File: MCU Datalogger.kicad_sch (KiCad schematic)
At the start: 25 parts, among them U1 24LC1025, U2 DS1337S+, U3 24LC1025, U4 ATMEGA328P-AU, Y1 32.768 KHz, Y2 16MHz

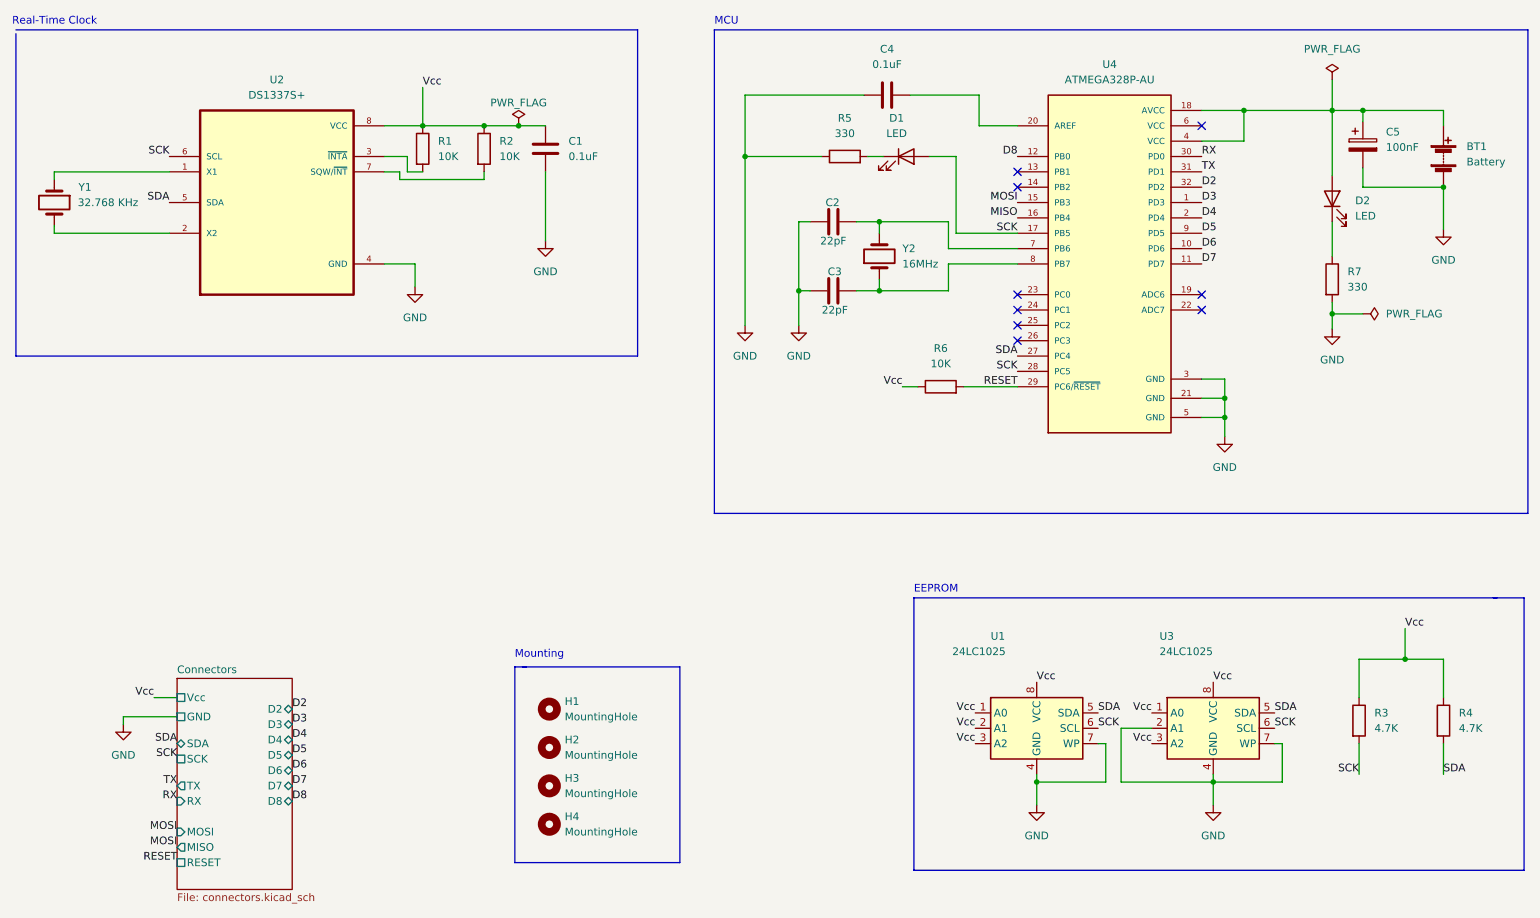
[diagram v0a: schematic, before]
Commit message: Fix schematic defect. SCK changed to SCL
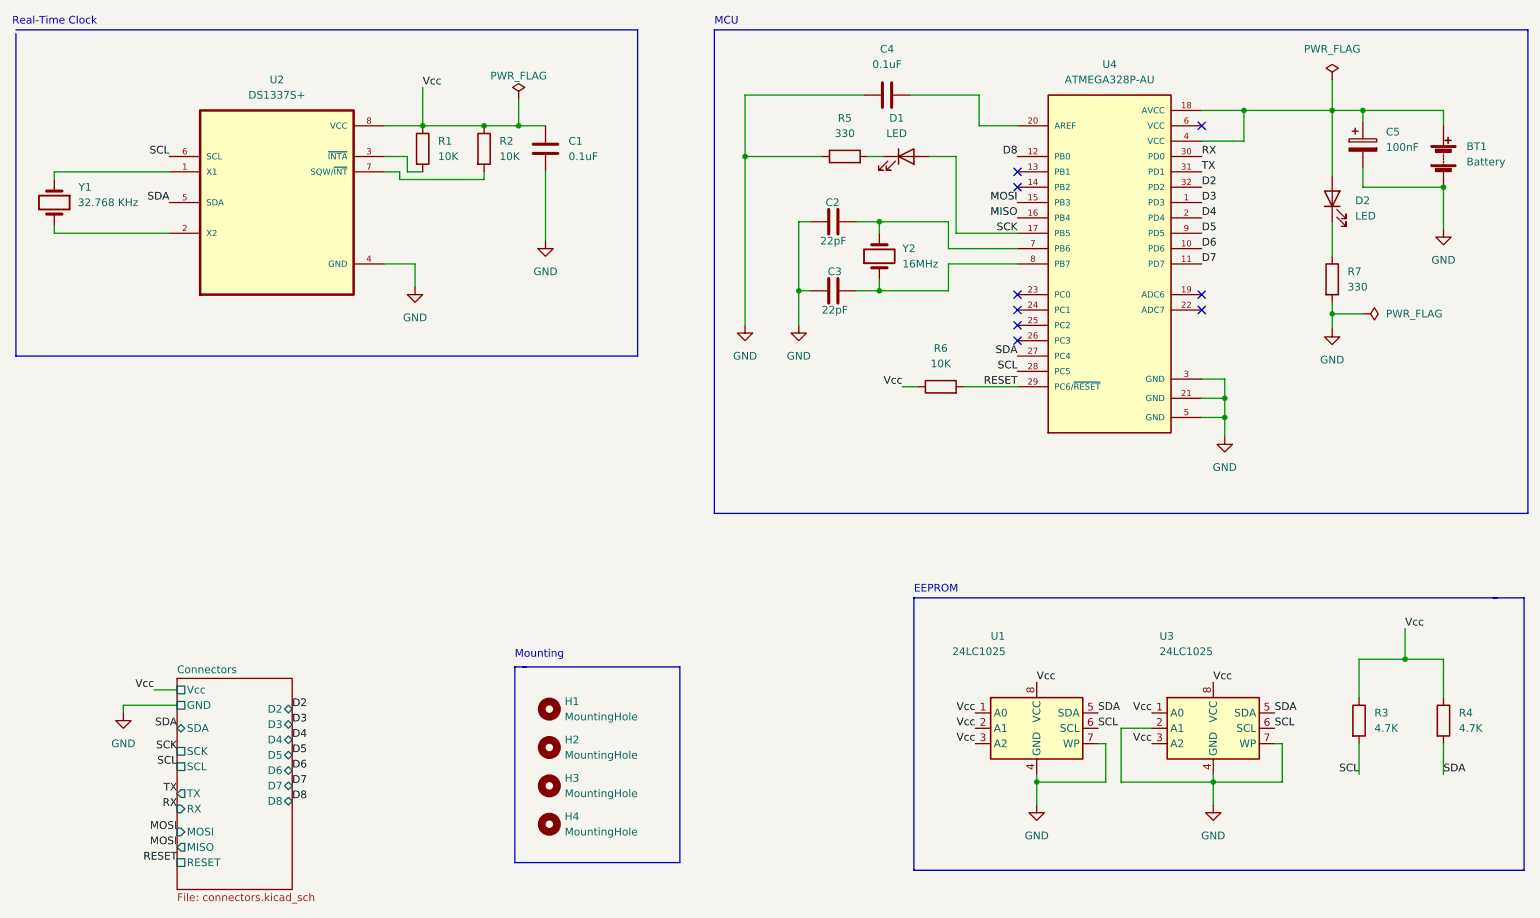
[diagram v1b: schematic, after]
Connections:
- net SCK: no longer R3.2, U1.6 (SCL), U2.6 (SCL), U3.6 (SCL), U4.28 (PC5)
- new net SCL: R3.2, U1.6 (SCL), U2.6 (SCL), U3.6 (SCL), U4.28 (PC5)
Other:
- sheet Connectors ports: added SCL; removed none
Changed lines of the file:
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@@
+    (stroke (width 0) (type default) (color 0 0 0 0))
+  )
+  (wire (pts (xy 107.315 34.29) (xy 107.315 38.735))
     (stroke (width 0) (type default) (color 0 0 0 0))
   )
@@
     (stroke (width 0) (type default) (color 0 0 0 0))
   )
+  (wire (pts (xy 41.91 135.89) (xy 41.91 134.62))
+    (stroke (width 0) (type default) (color 0 0 0 0))
+  )
   (wire (pts (xy 220.345 41.275) (xy 227.33 41.275))
     (stroke (width 0) (type default) (color 0 0 0 0))
@@
     (stroke (width 0) (type default) (color 0 0 0 0))
   )
-  (wire (pts (xy 50.8 136.525) (xy 41.91 136.525))
-    (stroke (width 0) (type default) (color 0 0 0 0))
-  )
   (wire (pts (xy 260.35 36.195) (xy 260.35 38.735))
     (stroke (width 0) (type default) (color 0 0 0 0))
@@
     (stroke (width 0) (type default) (color 0 0 0 0))
   )
+  (wire (pts (xy 41.91 134.62) (xy 50.8 134.62))
+    (stroke (width 0) (type default) (color 0 0 0 0))
+  )
   (wire (pts (xy 88.9 43.815) (xy 88.9 46.355))
     (stroke (width 0) (type default) (color 0 0 0 0))
@@
     (stroke (width 0) (type default) (color 0 0 0 0))
   )
-  (wire (pts (xy 41.91 136.525) (xy 41.91 137.795))
-    (stroke (width 0) (type default) (color 0 0 0 0))
-  )
   (polyline (pts (xy 133.985 128.27) (xy 133.985 160.655))
     (stroke (width 0) (type default) (color 0 0 0 0))
@@
     (stroke (width 0) (type default) (color 0 0 0 0))
   )
-  (wire (pts (xy 46.99 133.35) (xy 50.8 133.35))
+  (wire (pts (xy 46.99 132.08) (xy 50.8 132.08))
     (stroke (width 0) (type default) (color 0 0 0 0))
   )
@@
     (effects (font (size 1.27 1.27)) (justify left bottom))
   )
-  (label "SCK" (at 246.38 146.05 180)
-    (effects (font (size 1.27 1.27)) (justify right bottom))
-  )
   (label "TX" (at 220.345 46.355 0)
     (effects (font (size 1.27 1.27)) (justify left bottom))
@@
     (effects (font (size 1.27 1.27)) (justify right bottom))
   )
-  (label "SCK" (at 189.865 79.375 180)
+  (label "SCL" (at 189.865 79.375 180)
     (effects (font (size 1.27 1.27)) (justify right bottom))
   )
@@
     (effects (font (size 1.27 1.27)) (justify right bottom))
   )
-  (label "TX" (at 50.8 147.955 180)
+  (label "TX" (at 50.8 149.225 180)
     (effects (font (size 1.27 1.27)) (justify right bottom))
   )
@@
     (effects (font (size 1.27 1.27)) (justify left bottom))
   )
-  (label "SDA" (at 50.8 140.97 180)
+  (label "SDA" (at 50.8 138.43 180)
     (effects (font (size 1.27 1.27)) (justify right bottom))
   )
@@
     (effects (font (size 1.27 1.27)) (justify left bottom))
   )
+  (label "SCL" (at 232.41 138.43 0)
+    (effects (font (size 1.27 1.27)) (justify left bottom))
+  )
   (label "RESET" (at 189.865 81.915 180)
     (effects (font (size 1.27 1.27)) (justify right bottom))
@@
     (effects (font (size 1.27 1.27)) (justify left bottom))
   )
+  (label "SCL" (at 203.2 138.43 0)
+    (effects (font (size 1.27 1.27)) (justify left bottom))
+  )
   (label "MOSI" (at 189.865 51.435 180)
     (effects (font (size 1.27 1.27)) (justify right bottom))
@@
     (effects (font (size 1.27 1.27)) (justify right bottom))
   )
-  (label "SCK" (at 203.2 138.43 0)
-    (effects (font (size 1.27 1.27)) (justify left bottom))
-  )
   (label "SDA" (at 203.2 135.89 0)
     (effects (font (size 1.27 1.27)) (justify left bottom))
@@
     (effects (font (size 1.27 1.27)) (justify left bottom))
   )
-  (label "SCK" (at 49.53 43.815 180)
-    (effects (font (size 1.27 1.27)) (justify right bottom))
-  )
   (label "D3" (at 220.345 51.435 0)
     (effects (font (size 1.27 1.27)) (justify left bottom))
@@
     (effects (font (size 1.27 1.27)) (justify left bottom))
   )
+  (label "SCL" (at 246.38 146.05 180)
+    (effects (font (size 1.27 1.27)) (justify right bottom))
+  )
+  (label "SCL" (at 50.8 144.78 180)
+    (effects (font (size 1.27 1.27)) (justify right bottom))
+  )
+  (label "SCL" (at 49.53 43.815 180)
+    (effects (font (size 1.27 1.27)) (justify right bottom))
+  )
   (label "SCK" (at 189.865 56.515 180)
     (effects (font (size 1.27 1.27)) (justify right bottom))
@@
     (effects (font (size 1.27 1.27)) (justify left bottom))
   )
-  (label "Vcc" (at 46.99 133.35 180)
+  (label "Vcc" (at 46.99 132.08 180)
     (effects (font (size 1.27 1.27)) (justify right bottom))
   )
@@
     (effects (font (size 1.27 1.27)) (justify left bottom))
   )
-  (label "SCK" (at 50.8 143.51 180)
-    (effects (font (size 1.27 1.27)) (justify right bottom))
-  )
-  (label "RX" (at 50.8 150.495 180)
+  (label "RX" (at 50.8 151.765 180)
     (effects (font (size 1.27 1.27)) (justify right bottom))
   )
@@
     (effects (font (size 1.27 1.27)) (justify right bottom))
   )
-  (label "SCK" (at 232.41 138.43 0)
-    (effects (font (size 1.27 1.27)) (justify left bottom))
-  )
   (label "D7" (at 69.85 147.955 0)
     (effects (font (size 1.27 1.27)) (justify left bottom))
@@
     (effects (font (size 1.27 1.27)) (justify left bottom))
   )
+  (label "SCK" (at 50.8 142.24 180)
+    (effects (font (size 1.27 1.27)) (justify right bottom))
+  )
   (label "SDA" (at 260.35 146.05 0)
     (effects (font (size 1.27 1.27)) (justify left bottom))
@@
     (effects (font (size 1.27 1.27)) (justify left bottom))
   )
-  (symbol (lib_id "power:GND") (at 41.91 137.795 0) (unit 1)
-    (in_bom yes) (on_board yes) (fields_autoplaced)
-    (property "Reference" "#PWR0102" (id 0) (at 41.91 144.145 0)
-      (effects (font (size 1.27 1.27)) hide)
-    )
-    (property "Value" "GND" (id 1) (at 41.91 142.875 0))
-    (property "Footprint" "" (id 2) (at 41.91 137.795 0)
-      (effects (font (size 1.27 1.27)) hide)
-    )
-    (property "Datasheet" "" (id 3) (at 41.91 137.795 0)
+  (symbol (lib_id "power:GND") (at 41.91 135.89 0) (unit 1)
+    (in_bom yes) (on_board yes) (fields_autoplaced)
+    (property "Reference" "#PWR0102" (id 0) (at 41.91 142.24 0)
+      (effects (font (size 1.27 1.27)) hide)
+    )
+    (property "Value" "GND" (id 1) (at 41.91 140.97 0))
+    (property "Footprint" "" (id 2) (at 41.91 135.89 0)
+      (effects (font (size 1.27 1.27)) hide)
+    )
+    (property "Datasheet" "" (id 3) (at 41.91 135.89 0)
       (effects (font (size 1.27 1.27)) hide)
     )
@@
     (pin "1")
   )
-  (symbol (lib_id "power:PWR_FLAG") (at 107.315 38.735 0) (unit 1)
+  (symbol (lib_id "power:PWR_FLAG") (at 107.315 34.29 0) (unit 1)
     (in_bom yes) (on_board yes)
-    (property "Reference" "#FLG0103" (id 0) (at 107.315 36.83 0)
-      (effects (font (size 1.27 1.27)) hide)
-    )
-    (property "Value" "PWR_FLAG" (id 1) (at 107.315 34.925 0))
-    (property "Footprint" "" (id 2) (at 107.315 38.735 0)
-      (effects (font (size 1.27 1.27)) hide)
-    )
-    (property "Datasheet" "~" (id 3) (at 107.315 38.735 0)
+    (property "Reference" "#FLG0103" (id 0) (at 107.315 32.385 0)
+      (effects (font (size 1.27 1.27)) hide)
+    )
+    (property "Value" "PWR_FLAG" (id 1) (at 107.315 30.48 0))
+    (property "Footprint" "" (id 2) (at 107.315 34.29 0)
+      (effects (font (size 1.27 1.27)) hide)
+    )
+    (property "Datasheet" "~" (id 3) (at 107.315 34.29 0)
       (effects (font (size 1.27 1.27)) hide)
     )
@@
       (effects (font (size 1.27 1.27)) (justify left top))
     )
-    (pin "Vcc" passive (at 50.8 133.35 180)
-      (effects (font (size 1.27 1.27)) (justify left))
-    )
-    (pin "SDA" bidirectional (at 50.8 140.97 180)
-      (effects (font (size 1.27 1.27)) (justify left))
-    )
-    (pin "GND" passive (at 50.8 136.525 180)
-      (effects (font (size 1.27 1.27)) (justify left))
-    )
-    (pin "RX" input (at 50.8 150.495 180)
-      (effects (font (size 1.27 1.27)) (justify left))
-    )
-    (pin "TX" output (at 50.8 147.955 180)
+    (pin "Vcc" passive (at 50.8 132.08 180)
+      (effects (font (size 1.27 1.27)) (justify left))
+    )
+    (pin "SDA" bidirectional (at 50.8 138.43 180)
+      (effects (font (size 1.27 1.27)) (justify left))
+    )
+    (pin "GND" passive (at 50.8 134.62 180)
+      (effects (font (size 1.27 1.27)) (justify left))
+    )
+    (pin "RX" input (at 50.8 151.765 180)
+      (effects (font (size 1.27 1.27)) (justify left))
+    )
+    (pin "TX" output (at 50.8 149.225 180)
       (effects (font (size 1.27 1.27)) (justify left))
     )
@@
       (effects (font (size 1.27 1.27)) (justify left))
     )
-    (pin "SCK" passive (at 50.8 143.51 180)
-      (effects (font (size 1.27 1.27)) (justify left))
-    )
     (pin "D2" bidirectional (at 69.85 135.255 0)
       (effects (font (size 1.27 1.27)) (justify right))
@@
       (effects (font (size 1.27 1.27)) (justify left))
     )
+    (pin "SCK" passive (at 50.8 142.24 180)
+      (effects (font (size 1.27 1.27)) (justify left))
+    )
+    (pin "SCL" passive (at 50.8 144.78 180)
+      (effects (font (size 1.27 1.27)) (justify left))
+    )
